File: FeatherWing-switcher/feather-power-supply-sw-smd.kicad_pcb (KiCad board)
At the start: 2 copper layers, 9 parts, among them J4 QWIIC, J5 0.1, Q1 Q_PMOS_GSD

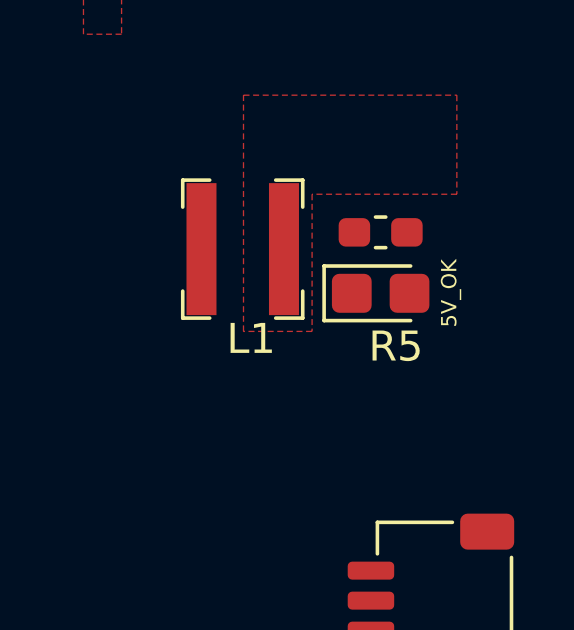
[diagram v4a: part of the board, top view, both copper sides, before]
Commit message: minor bom consolidation
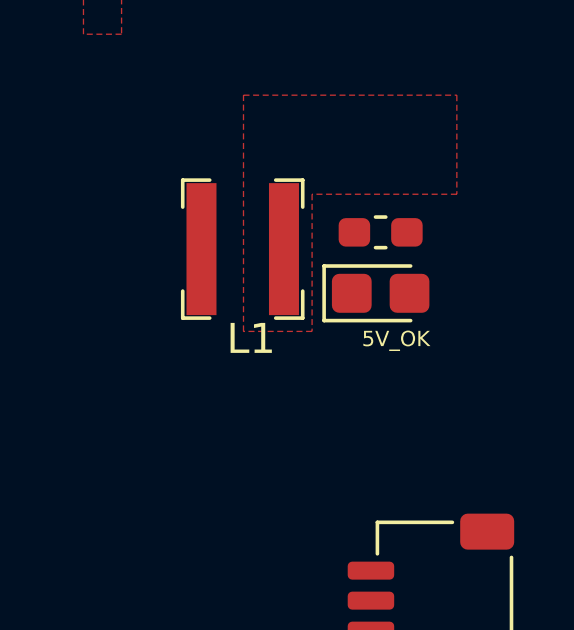
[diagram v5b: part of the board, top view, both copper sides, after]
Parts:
- moved REF** 1.78 mm to (140.2, 85.1)
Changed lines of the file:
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@@
     (34 B.Paste user)
     (35 F.Paste user)
-    (36 B.SilkS user hide)
+    (36 B.SilkS user)
     (37 F.SilkS user)
     (38 B.Mask user)
@@
   )
   (setup
-    (last_trace_width 1.2192)
+    (last_trace_width 0.1524)
     (user_trace_width 0.1524)
     (user_trace_width 0.3048)
@@
   )
   (module Symbol:KiCad-Logo2_5mm_SilkScreen (layer B.Cu)
-    (at 138.43 85.09 180)
+    (at 140.208 85.09 180)
     (descr "KiCad Logo")
     (tags "Logo KiCad")
@@
     (tags "resistor handsolder")
     (attr smd)
-    (fp_text reference R5 (at 0.508 3.81 180) (layer F.SilkS)
+    (fp_text reference R5 (at 0.508 3.81 180) (layer F.SilkS) hide
       (effects (font (size 1 1) (thickness 0.15)))
     )
@@
       (effects (font (size 1 1) (thickness 0.15)))
     )
-    (fp_text value 5V_OK (at 2.286 0 90) (layer F.SilkS)
+    (fp_text value 5V_OK (at 0.508 1.524) (layer F.SilkS)
       (effects (font (size 0.508 0.508) (thickness 0.127)))
     )
@@
       (effects (font (size 1 1) (thickness 0.15)))
     )
-    (fp_text value 100K/0.1% (at 0 1.43) (layer F.Fab)
+    (fp_text value 10K (at 0 1.43) (layer F.Fab)
       (effects (font (size 1 1) (thickness 0.15)))
     )
@@
       (effects (font (size 1 1) (thickness 0.15)))
     )
-    (fp_text value 10k (at 0 1.43) (layer F.Fab)
+    (fp_text value 10K (at 0 1.43) (layer F.Fab)
       (effects (font (size 1 1) (thickness 0.15)))
     )
@@
       (effects (font (size 1 1) (thickness 0.15)))
     )
-    (fp_text value 1M/0.1% (at 0 1.43) (layer F.Fab)
+    (fp_text value 100K (at 0 1.43) (layer F.Fab)
       (effects (font (size 1 1) (thickness 0.15)))
     )
@@
   (via (at 147.066 70.866) (size 0.6858) (drill 0.3302) (layers F.Cu B.Cu) (net 2))
   (via (at 147.066 72.136) (size 0.6858) (drill 0.3302) (layers F.Cu B.Cu) (net 2))
-  (via (at 136.906 91.948) (size 0.6858) (drill 0.3302) (layers F.Cu B.Cu) (net 2))
-  (via (at 139.446 91.948) (size 0.6858) (drill 0.3302) (layers F.Cu B.Cu) (net 2))
-  (via (at 134.366 91.948) (size 0.6858) (drill 0.3302) (layers F.Cu B.Cu) (net 2))
-  (via (at 136.906 93.472) (size 0.6858) (drill 0.3302) (layers F.Cu B.Cu) (net 2))
-  (via (at 139.446 93.472) (size 0.6858) (drill 0.3302) (layers F.Cu B.Cu) (net 2))
-  (via (at 134.366 93.472) (size 0.6858) (drill 0.3302) (layers F.Cu B.Cu) (net 2))
-  (via (at 136.906 94.996) (size 0.6858) (drill 0.3302) (layers F.Cu B.Cu) (net 2))
-  (via (at 139.446 94.996) (size 0.6858) (drill 0.3302) (layers F.Cu B.Cu) (net 2))
-  (via (at 134.366 94.996) (size 0.6858) (drill 0.3302) (layers F.Cu B.Cu) (net 2))
-  (via (at 136.906 96.52) (size 0.6858) (drill 0.3302) (layers F.Cu B.Cu) (net 2))
-  (via (at 134.366 96.52) (size 0.6858) (drill 0.3302) (layers F.Cu B.Cu) (net 2))
-  (via (at 139.446 96.52) (size 0.6858) (drill 0.3302) (layers F.Cu B.Cu) (net 2))
-  (via (at 136.906 99.568) (size 0.6858) (drill 0.3302) (layers F.Cu B.Cu) (net 2))
-  (via (at 139.446 98.044) (size 0.6858) (drill 0.3302) (layers F.Cu B.Cu) (net 2))
-  (via (at 136.906 98.044) (size 0.6858) (drill 0.3302) (layers F.Cu B.Cu) (net 2))
-  (via (at 134.366 99.568) (size 0.6858) (drill 0.3302) (layers F.Cu B.Cu) (net 2))
-  (via (at 134.366 98.044) (size 0.6858) (drill 0.3302) (layers F.Cu B.Cu) (net 2))
-  (via (at 139.446 99.568) (size 0.6858) (drill 0.3302) (layers F.Cu B.Cu) (net 2))
-  (via (at 141.986 91.948) (size 0.6858) (drill 0.3302) (layers F.Cu B.Cu) (net 2))
-  (via (at 141.986 99.568) (size 0.6858) (drill 0.3302) (layers F.Cu B.Cu) (net 2))
-  (via (at 141.986 94.996) (size 0.6858) (drill 0.3302) (layers F.Cu B.Cu) (net 2))
-  (via (at 141.986 98.044) (size 0.6858) (drill 0.3302) (layers F.Cu B.Cu) (net 2))
-  (via (at 141.986 96.52) (size 0.6858) (drill 0.3302) (layers F.Cu B.Cu) (net 2))
-  (via (at 141.986 93.472) (size 0.6858) (drill 0.3302) (layers F.Cu B.Cu) (net 2))
+  (via (at 136.398 91.694) (size 0.6858) (drill 0.3302) (layers F.Cu B.Cu) (net 2))
+  (via (at 138.938 91.694) (size 0.6858) (drill 0.3302) (layers F.Cu B.Cu) (net 2))
+  (via (at 133.858 91.694) (size 0.6858) (drill 0.3302) (layers F.Cu B.Cu) (net 2))
+  (via (at 136.398 93.218) (size 0.6858) (drill 0.3302) (layers F.Cu B.Cu) (net 2))
+  (via (at 138.938 93.218) (size 0.6858) (drill 0.3302) (layers F.Cu B.Cu) (net 2))
+  (via (at 133.858 93.218) (size 0.6858) (drill 0.3302) (layers F.Cu B.Cu) (net 2))
+  (via (at 136.398 94.742) (size 0.6858) (drill 0.3302) (layers F.Cu B.Cu) (net 2))
+  (via (at 138.938 94.742) (size 0.6858) (drill 0.3302) (layers F.Cu B.Cu) (net 2))
+  (via (at 133.858 94.742) (size 0.6858) (drill 0.3302) (layers F.Cu B.Cu) (net 2))
+  (via (at 136.398 96.266) (size 0.6858) (drill 0.3302) (layers F.Cu B.Cu) (net 2))
+  (via (at 133.858 96.266) (size 0.6858) (drill 0.3302) (layers F.Cu B.Cu) (net 2))
+  (via (at 138.938 96.266) (size 0.6858) (drill 0.3302) (layers F.Cu B.Cu) (net 2))
+  (via (at 136.398 99.314) (size 0.6858) (drill 0.3302) (layers F.Cu B.Cu) (net 2))
+  (via (at 138.938 97.79) (size 0.6858) (drill 0.3302) (layers F.Cu B.Cu) (net 2))
+  (via (at 136.398 97.79) (size 0.6858) (drill 0.3302) (layers F.Cu B.Cu) (net 2))
+  (via (at 133.858 99.314) (size 0.6858) (drill 0.3302) (layers F.Cu B.Cu) (net 2))
+  (via (at 133.858 97.79) (size 0.6858) (drill 0.3302) (layers F.Cu B.Cu) (net 2))
+  (via (at 138.938 99.314) (size 0.6858) (drill 0.3302) (layers F.Cu B.Cu) (net 2))
+  (via (at 141.478 91.694) (size 0.6858) (drill 0.3302) (layers F.Cu B.Cu) (net 2))
+  (via (at 141.478 99.314) (size 0.6858) (drill 0.3302) (layers F.Cu B.Cu) (net 2))
+  (via (at 141.478 94.742) (size 0.6858) (drill 0.3302) (layers F.Cu B.Cu) (net 2))
+  (via (at 141.478 97.79) (size 0.6858) (drill 0.3302) (layers F.Cu B.Cu) (net 2))
+  (via (at 141.478 96.266) (size 0.6858) (drill 0.3302) (layers F.Cu B.Cu) (net 2))
+  (via (at 141.478 93.218) (size 0.6858) (drill 0.3302) (layers F.Cu B.Cu) (net 2))
   (via (at 142.24 79.502) (size 0.6858) (drill 0.3302) (layers F.Cu B.Cu) (net 2))
   (via (at 143.51 79.502) (size 0.6858) (drill 0.3302) (layers F.Cu B.Cu) (net 2))

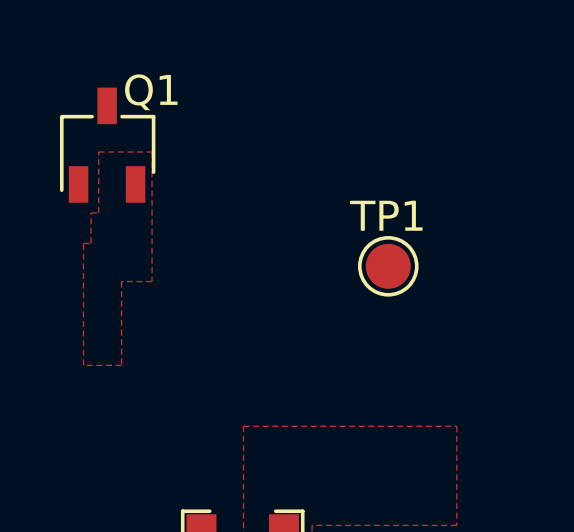
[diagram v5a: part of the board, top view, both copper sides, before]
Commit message: reduce ground pour clearance
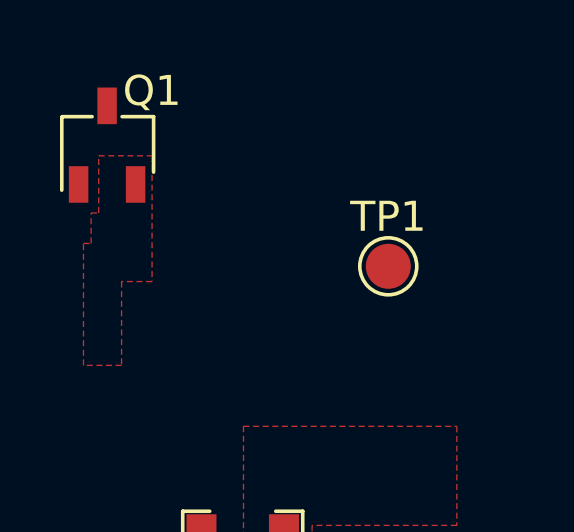
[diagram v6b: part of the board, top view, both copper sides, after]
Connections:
- net VUSB renamed +5V

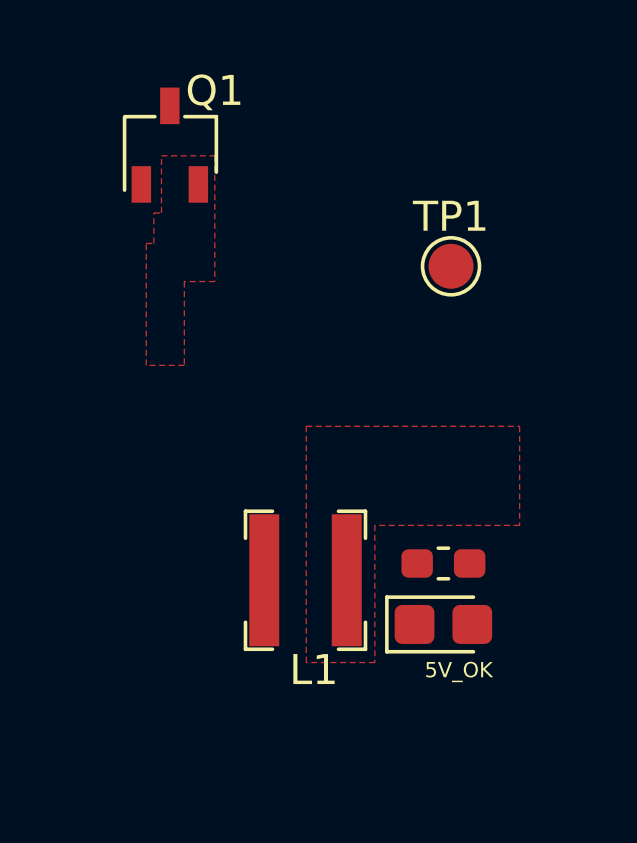
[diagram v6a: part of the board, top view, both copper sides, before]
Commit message: updates pad clearance and bom
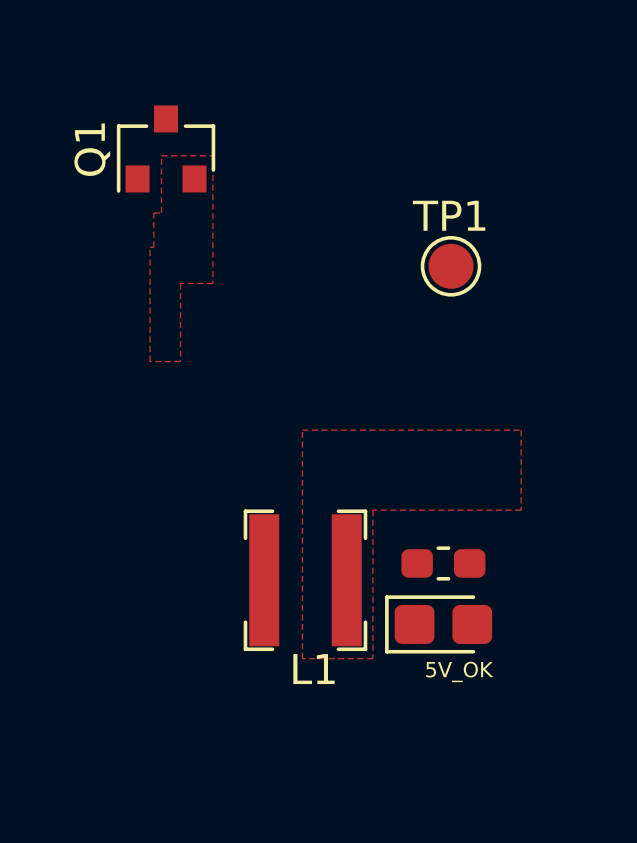
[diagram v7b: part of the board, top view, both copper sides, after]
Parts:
- Q1: footprint Package_TO_SOT_SMD:TSOT-23 -> Package_TO_SOT_SMD:SOT-23
- moved Q1 0.18 mm to (136.8, 73.3)
